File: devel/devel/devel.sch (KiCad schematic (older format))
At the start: 1 part

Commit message: Worked on the dev-board
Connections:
- net VDD: no longer A1.2 (IOREF)
- net NC: no longer names the net of A1.8 (VIN)
- net P.025 renamed P0.25
- no-connect marks 0 -> 2

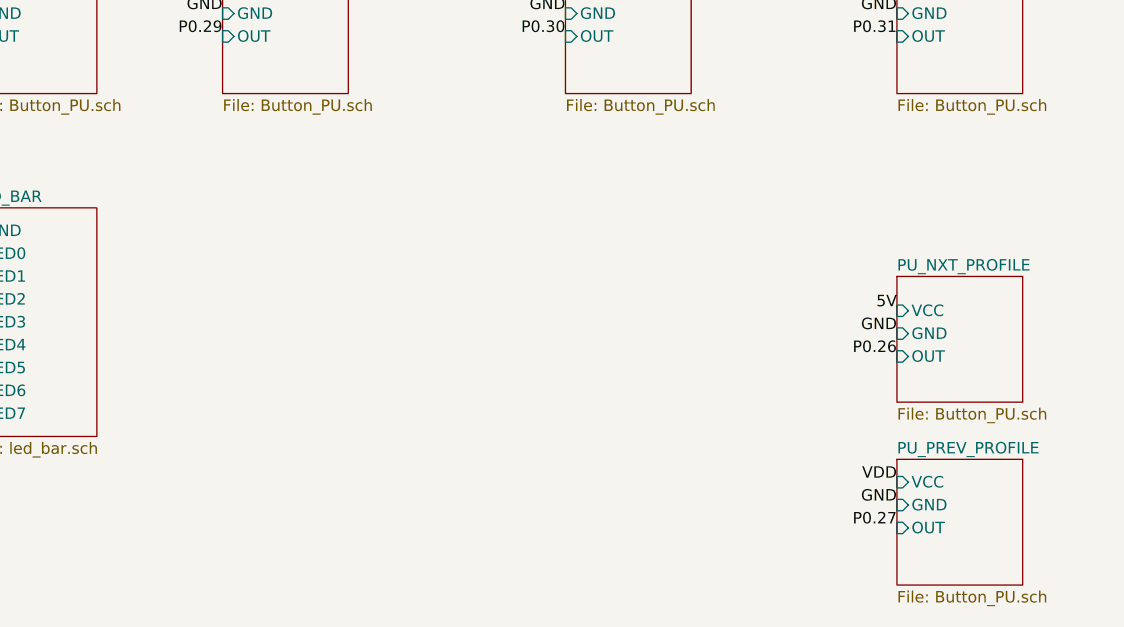
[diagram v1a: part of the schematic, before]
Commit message: Make a physical border
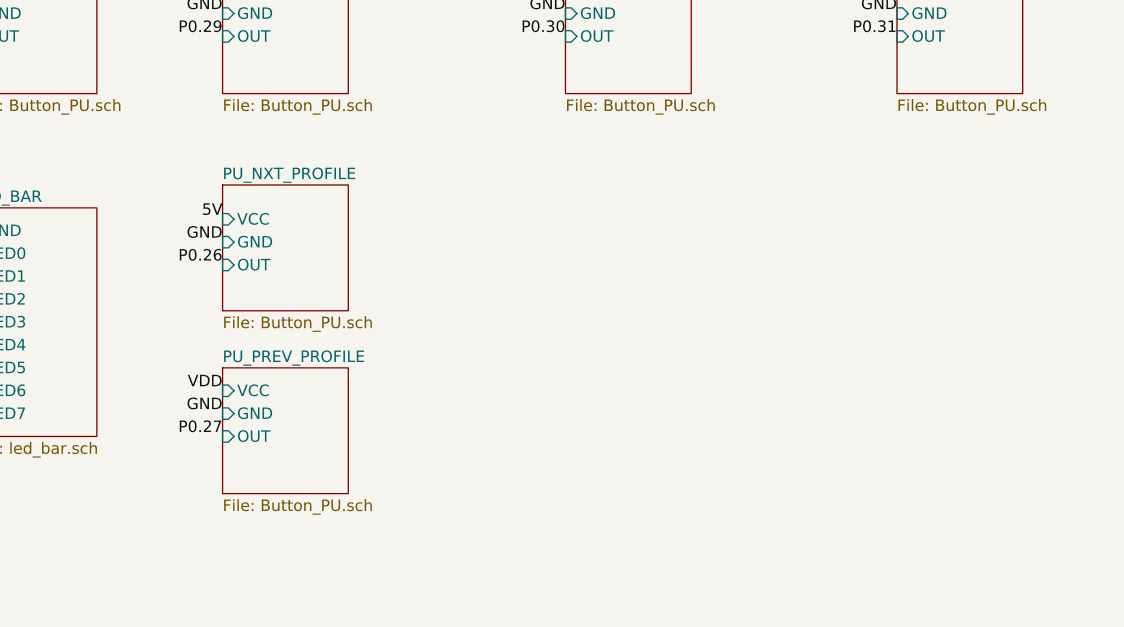
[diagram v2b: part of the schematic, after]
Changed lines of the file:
@@
 EESchema Schematic File Version 4
+LIBS:devel-cache
 EELAYER 26 0
 EELAYER END
@@
 Text Label 6100 1350 2    50   ~ 0
 P0.02
-Text Label 10150 3500 2    50   ~ 0
+Text Label 7200 3100 2    50   ~ 0
 P0.26
-Text Label 10150 4250 2    50   ~ 0
+Text Label 7200 3850 2    50   ~ 0
 P0.27
 Text Label 4500 3150 2    50   ~ 0
@@
 GND
 $Sheet
-S 10150 3150 550  550
+S 7200 2750 550  550
 U 5C59450C
 F0 "PU_NXT_PROFILE" 50
 F1 "Button_PU.sch" 50
-F2 "VCC" I L 10150 3300 50
-F3 "GND" I L 10150 3400 50
-F4 "OUT" I L 10150 3500 50
-$EndSheet
-$Sheet
-S 10150 3950 550  550
+F2 "VCC" I L 7200 2900 50
+F3 "GND" I L 7200 3000 50
+F4 "OUT" I L 7200 3100 50
+$EndSheet
+$Sheet
+S 7200 3550 550  550
 U 5C594511
 F0 "PU_PREV_PROFILE" 50
 F1 "Button_PU.sch" 50
-F2 "VCC" I L 10150 4050 50
-F3 "GND" I L 10150 4150 50
-F4 "OUT" I L 10150 4250 50
-$EndSheet
-Text Label 10150 3300 2    50   ~ 0
-5V
-Text Label 10150 3400 2    50   ~ 0
-GND
-Text Label 10150 4050 2    50   ~ 0
-VDD
-Text Label 10150 4150 2    50   ~ 0
-GND
-$Sheet
+F2 "VCC" I L 7200 3650 50
+F3 "GND" I L 7200 3750 50
+F4 "OUT" I L 7200 3850 50
+$EndSheet
+Text Label 7200 2900 2    50   ~ 0
+5V
+Text Label 7200 3000 2    50   ~ 0
+GND
+Text Label 7200 3650 2    50   ~ 0
+VDD
+Text Label 7200 3750 2    50   ~ 0
+GND
+$Sheet

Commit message: Preliminary placement and orientation of components to fit the board
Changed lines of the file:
@@
 $EndSheet
 Text Label 3400 1150 2    50   ~ 0
-5V
+VDD
 Text Label 3400 1250 2    50   ~ 0
 GND
@@
 $EndSheet
 Text Label 4500 1150 2    50   ~ 0
-5V
+VDD
 Text Label 4500 1250 2    50   ~ 0
 GND
@@
 $EndSheet
 Text Label 6100 1150 2    50   ~ 0
-5V
+VDD
 Text Label 6100 1250 2    50   ~ 0
 GND
@@
 $EndSheet
 Text Label 7200 1150 2    50   ~ 0
-5V
+VDD
 Text Label 7200 1250 2    50   ~ 0
 GND
@@
 $EndSheet
 Text Label 8700 1150 2    50   ~ 0
-5V
+VDD
 Text Label 8700 1250 2    50   ~ 0
 GND
@@
 $EndSheet
 Text Label 10150 1150 2    50   ~ 0
-5V
+VDD
 Text Label 10150 1250 2    50   ~ 0
 GND
@@
 GND
 Text Label 3400 1350 2    50   ~ 0
-P0.19
+P0.02
 Text Label 3400 2100 2    50   ~ 0
-P0.20
+P0.29
 Text Label 4500 1350 2    50   ~ 0
-P0.22
+P0.04
 Text Label 4500 2100 2    50   ~ 0
-P0.23
+P0.28
 Text Label 6100 3450 2    50   ~ 0
 P0.15
@@
 P0.03(A0)
 Text Label 6100 2100 2    50   ~ 0
-P0.04
+P0.22
 Text Label 7200 1350 2    50   ~ 0
-P0.28
+P0.23
 Text Label 7200 2100 2    50   ~ 0
-P0.29
+P0.20
 Text Label 8700 2100 2    50   ~ 0
 P0.30
@@
 P0.31
 Text Label 6100 1350 2    50   ~ 0
-P0.02
+P0.19
 Text Label 7200 3100 2    50   ~ 0
+P0.27
+Text Label 7200 3850 2    50   ~ 0
 P0.26
-Text Label 7200 3850 2    50   ~ 0
-P0.27
 Text Label 4500 3150 2    50   ~ 0
 RESET
@@
 $EndSheet
 Text Label 7200 2900 2    50   ~ 0
-5V
+VDD
 Text Label 7200 3000 2    50   ~ 0
 GND

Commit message: Made Gustav's design into a double sided board
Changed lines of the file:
@@
 Text Label 10150 2000 2    50   ~ 0
 GND
+Text Label 10150 2100 2    50   ~ 0
+P0.02
 Text Label 3400 1350 2    50   ~ 0
-P0.02
-Text Label 3400 2100 2    50   ~ 0
 P0.29
-Text Label 4500 1350 2    50   ~ 0
+Text Label 10150 1350 2    50   ~ 0
 P0.04
 Text Label 4500 2100 2    50   ~ 0
@@
 Text Label 8700 1350 2    50   ~ 0
 P0.24
-Text Label 10150 1350 2    50   ~ 0
+Text Label 8700 2100 2    50   ~ 0
 P0.25
 Text Label 3400 3150 2    50   ~ 0
@@
 Text Label 6100 2100 2    50   ~ 0
 P0.22
+Text Label 6100 1350 2    50   ~ 0
+P0.23
 Text Label 7200 1350 2    50   ~ 0
-P0.23
+P0.20
+Text Label 4500 1350 2    50   ~ 0
+P0.30
+Text Label 3400 2100 2    50   ~ 0
+P0.31
 Text Label 7200 2100 2    50   ~ 0
-P0.20
-Text Label 8700 2100 2    50   ~ 0
-P0.30
-Text Label 10150 2100 2    50   ~ 0
-P0.31
-Text Label 6100 1350 2    50   ~ 0
 P0.19
+Text Label 7200 3850 2    50   ~ 0
+P0.27
 Text Label 7200 3100 2    50   ~ 0
-P0.27
-Text Label 7200 3850 2    50   ~ 0
 P0.26
 Text Label 4500 3150 2    50   ~ 0
